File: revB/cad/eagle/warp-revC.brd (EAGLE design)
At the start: 38.1 x 38.1 mm, 148 parts, among them J3 QIIC connector, J4 DF40FC-20DP-0.4V(51)

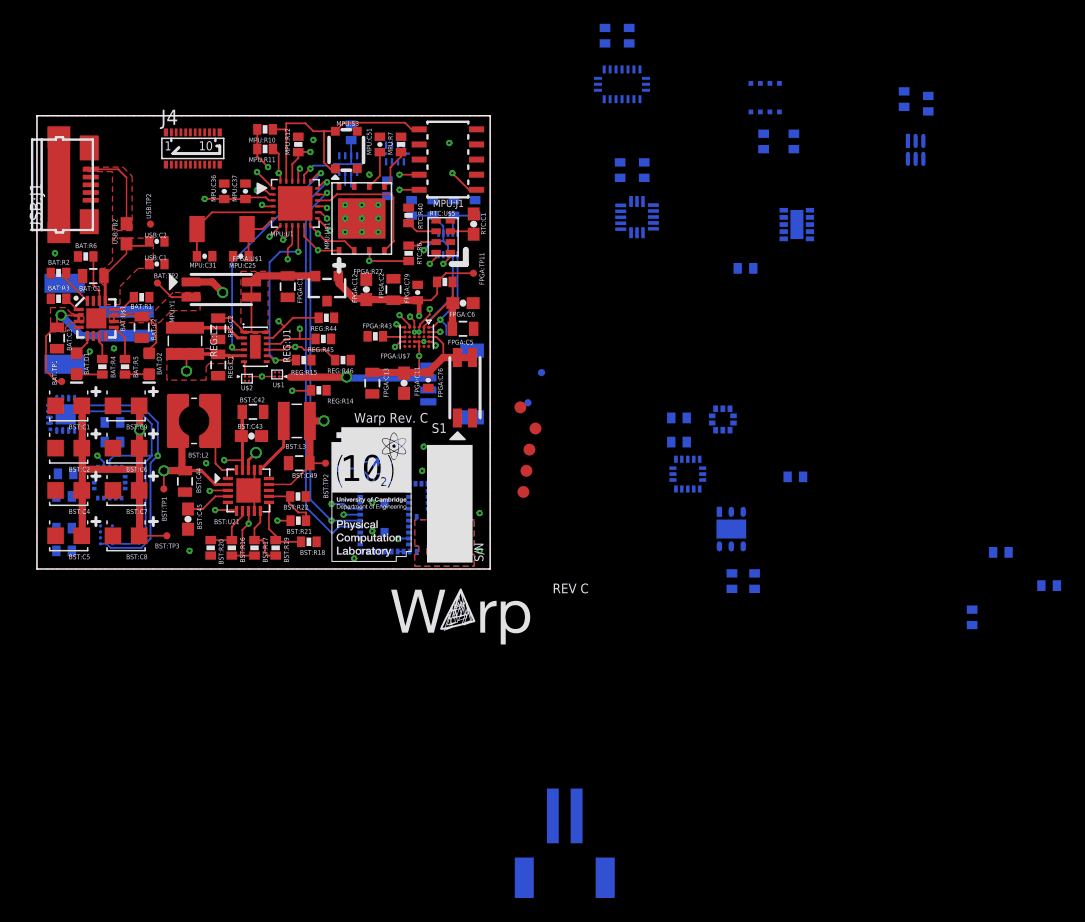
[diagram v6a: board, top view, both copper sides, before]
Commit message: Bottom sensor placement
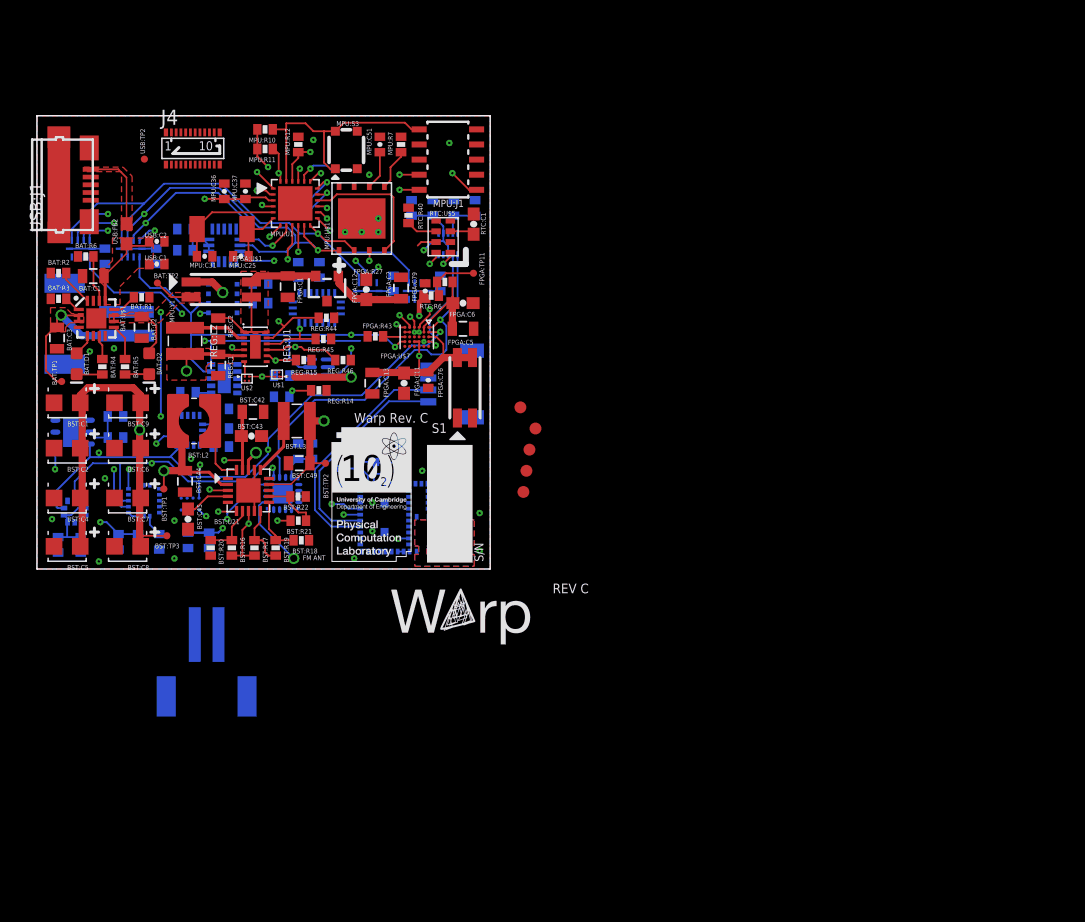
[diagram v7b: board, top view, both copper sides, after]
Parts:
- removed SEN1:C52, SEN1:C53: 0.1uF, SparkFun-Passives:0402-CAP
- removed SEN1:U20, SEN1:U23: ISL23415UTQFN, ISL23415:ISL23415
- removed SEN2:TP1, SEN2:TP2: TPTP06R, testpad:TP06R
- added DP:C1, DP:C2, DP:C52, DP:C53: 0.1uF, SparkFun-Passives:0402-CAP
- added DP:U1, DP:U2, DP:U20, DP:U23: ISL23415UTQFN, ISL23415:ISL23415
- moved SEN2:C46 70.8 mm to (15.5, 11.8)
- moved SEN2:C24 68.6 mm to (10.3, 2.29), turned to 270 degrees
- moved SEN2:C47 66.6 mm to (15.5, 13.5)
- moved SEN1:C28 59.7 mm to (20.6, 14.5), turned to 0 degrees
- moved SEN1:C29 57.3 mm to (20.6, 16.3), turned to 0 degrees
- moved SEN2:U9 56.0 mm to (3.05, 11.6), turned to 180 degrees
- moved SEN2:C22 55.1 mm to (6.60, 11.0), turned to 180 degrees
- moved SEN2:U16 55.0 mm to (3.17, 4.83)
- moved SEN2:C23 53.6 mm to (6.60, 12.8), turned to 180 degrees
- moved SEN1:U10 53.4 mm to (23.7, 17.0), turned to 180 degrees
- moved SEN2:C18 53.3 mm to (1.78, 2.03), turned to 270 degrees
- moved SEN2:C19 51.0 mm to (3.68, 2.03), turned to 270 degrees
- moved SEN1:U5 49.8 mm to (15.7, 16.0), turned to 0 degrees
- moved SEN1:U2 48.6 mm to (15.6, 22.7), turned to 0 degrees
- moved SEN2:C14 48.3 mm to (15.5, 10.3)
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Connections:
- removed net SEN2:SI4705_LPI: SEN2:TP1.TP, SEN2:U13.P$4
- removed net SI4705_!RST!: MPU:U1.P$14
- new net DP:ISL23415_SPI_CS: DP:U1.4, DP:U2.4, DP:U20.4, DP:U23.4
- net GND: now also DP:C1.2, DP:C2.2, DP:C52.2, DP:C53.2, DP:U1.9, DP:U2.9, DP:U20.9, DP:U23.9; no longer SEN1:C52.2, SEN1:C53.2, SEN1:U20.9, SEN1:U23.9
- net I2C1_SCL: now also DP:U20.6; no longer SEN1:U20.6
- net I2C1_SDA: now also DP:U23.6; no longer SEN1:U23.6
- net I2C2_SCL: now also DP:U1.6
- net I2C2_SDA: now also DP:U2.6
- net ISL23415_SPI_CS: no longer SEN1:U20.4, SEN1:U23.4
- net SEN2:SI4705_FMI: no longer SEN2:TP2.TP
- net SI4705_!RST: now also MPU:U1.P$14
- net SPI_MISO/UART_RTS: now also DP:U1.2, DP:U2.2, DP:U20.2, DP:U23.2; no longer SEN1:U20.2, SEN1:U23.2
- net SPI_MOSI/UART_CTS: now also DP:U1.3, DP:U2.3, DP:U20.3, DP:U23.3; no longer SEN1:U20.3, SEN1:U23.3
- net SPI_SCK: now also DP:U1.1, DP:U2.1, DP:U20.1, DP:U23.1; no longer SEN1:U20.1, SEN1:U23.1
- net VS2: now also DP:C1.1, DP:C2.1, DP:C52.1, DP:C53.1, DP:U1.10, DP:U1.5, DP:U1.8, DP:U2.10, DP:U2.5, DP:U2.8, DP:U20.10, DP:U20.5, DP:U20.8, DP:U23.10, DP:U23.5, DP:U23.8; no longer SEN1:C52.1, SEN1:C53.1, SEN1:U20.10, SEN1:U20.5, SEN1:U20.8, SEN1:U23.10, SEN1:U23.5, SEN1:U23.8
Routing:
- net VS2: track 22.3 -> 68.2 mm, vias 3 -> 6
- net SI4705_!RST: track 0.00 -> 42.8 mm, vias 0 -> 4
- net SPI_SCK: track 16.4 -> 58.5 mm
- net SPI_MISO/UART_RTS: track 36.5 -> 74.6 mm, vias 3 -> 6
- net I2C1_SDA: track 1.01 -> 38.4 mm, vias 1 -> 3
- net SPI_MOSI/UART_CTS: track 39.0 -> 75.9 mm, vias 3 -> 6
- net CLK32K: track 1.13 -> 35.6 mm
- net I2C1_SCL: track 0.73 -> 34.4 mm, vias 1 -> 4
- net I2C2_SCL: track 35.2 -> 68.7 mm, vias 3 -> 7
- net I2C2_SDA: track 32.2 -> 64.5 mm, vias 1 -> 4
- net REG_CTRL: track 28.2 -> 10.5 mm
- net REG_VSEL4: track 16.1 -> 4.83 mm
- net I2C0_SDA/UART_RX: track 36.0 -> 24.8 mm
- net I2C0_SCL/UART_TX: track 33.3 -> 22.6 mm, vias 3 -> 2
- net ADXL362_SPI_CS: track 0.87 -> 10.4 mm, vias 1 -> 2
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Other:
- board text added: "FM ANT"

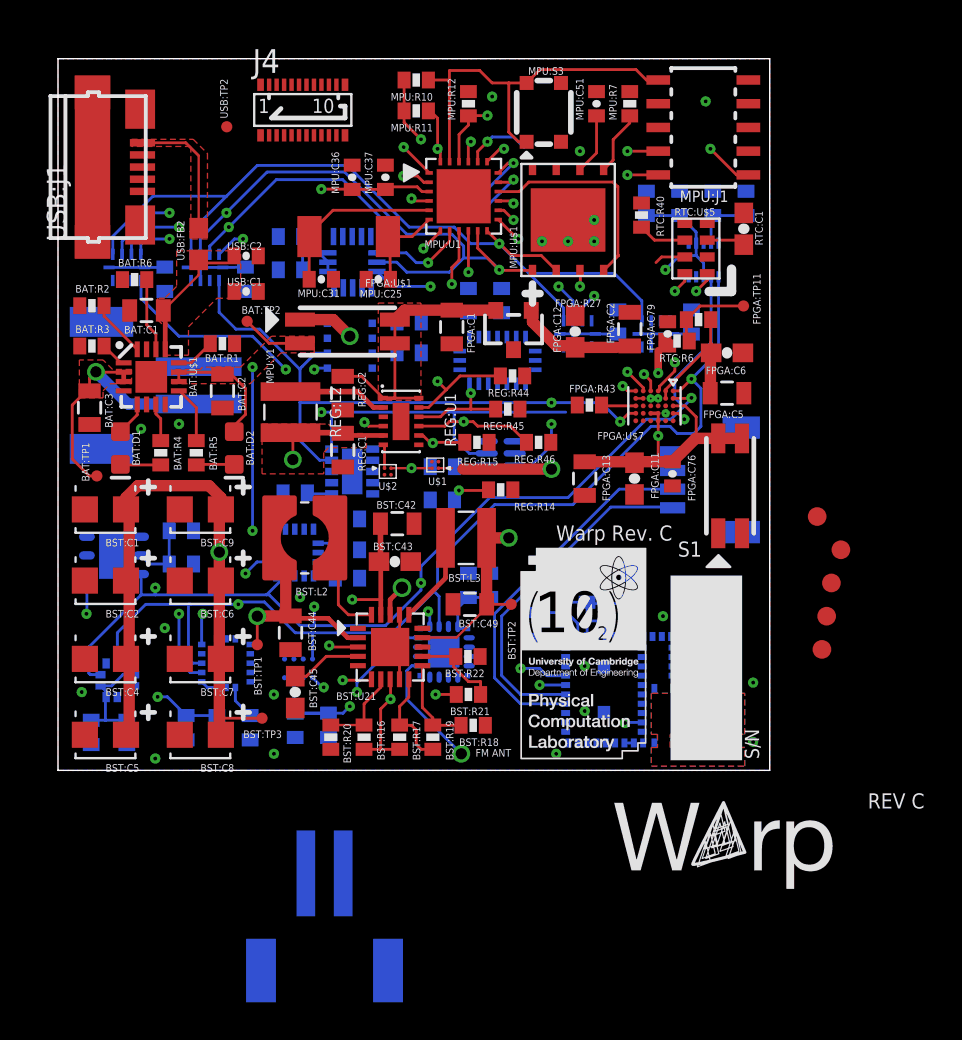
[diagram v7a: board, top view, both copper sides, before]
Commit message: All chips routed
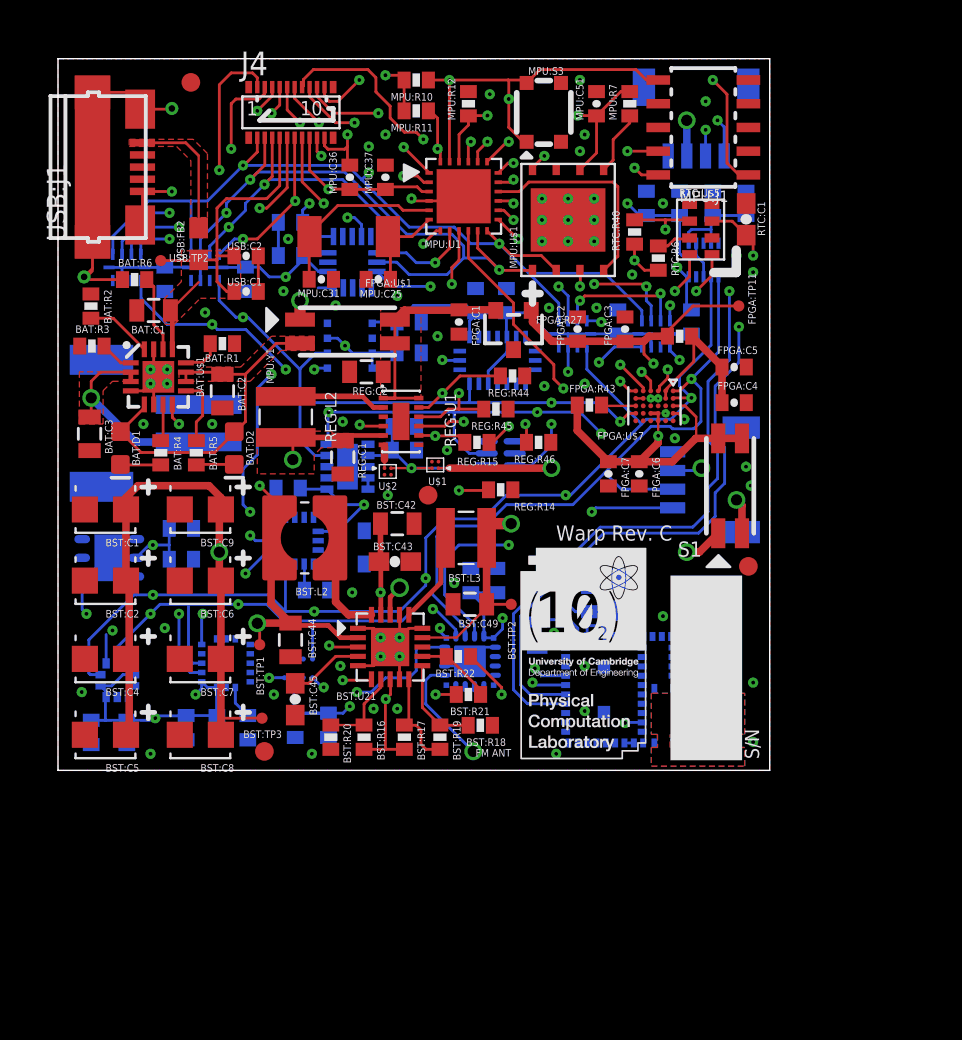
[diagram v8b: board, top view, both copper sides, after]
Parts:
- removed BAT:TP1, BAT:TP2: TPSTP06R, testpad:TP06R
- removed FD4: FIDUCIAL1X2, SparkFun-Aesthetics:FIDUCIAL-1X2
- removed FPGA:C11, FPGA:C12: 0.1uF, SparkFun-Passives:0603-CAP
- removed FPGA:C13: 1uF, SparkFun-Passives:0805
- removed FPGA:C76, FPGA:C79: 10nF, SparkFun-Passives:0402-CAP
- added FPGA:C3, FPGA:C4: 0.1uF, SparkFun-Passives:0402-CAP
- added FPGA:C7: 10uF, SparkFun-Passives:0402-CAP
- FPGA:C1, FPGA:C2, FPGA:C5: device SparkFun-Passives:0805 -> SparkFun-Passives:0402-CAP
- FPGA:C6: device SparkFun-Passives:0603-CAP -> SparkFun-Passives:0402-CAP
- J2: value (none) -> QIIC connector; device SparkFun-Connectors:JST-2-SMD -> SparkX:1X04_1MM_RA
- moved J2 46.6 mm to (34.2, 32.9)
- moved FD1 40.8 mm to (7.11, 36.8)
- moved FD5 31.7 mm to (11.0, 1.02)
- moved FD2 22.3 mm to (19.8, 14.7)
- moved FPGA:C6 8.00 mm to (31.1, 15.9), turned to 270 degrees
- moved USB:TP2 7.99 mm to (5.50, 27.3), turned to 270 degrees
- moved FD3 5.03 mm to (37.0, 10.9)
- moved RTC:R6 4.55 mm to (32.1, 27.4), turned to 270 degrees
- moved SEN1:C28 3.35 mm to (18.5, 17.1), turned to 180 degrees
- moved SEN1:C29 2.96 mm to (18.5, 18.4), turned to 180 degrees
- moved FPGA:C2 2.79 mm to (27.8, 23.6)
- moved SEN2:C47 2.43 mm to (15.7, 11.0)
- moved J1 2.03 mm to (3.83, 18.6)
- moved SEN2:C14 1.77 mm to (13.8, 9.65)
- moved REG:C2 1.71 mm to (16.5, 21.3), turned to 180 degrees
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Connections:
- removed net DP:ISL23415_SPI_CS: DP:U1.4, DP:U2.4, DP:U20.4, DP:U23.4
- net ADXL362_SPI_CS: no longer J4.P$18
- net BAT: no longer BAT:TP1.TP
- net BGX13S_!RST: now also J4.P$7; no longer J4.P$20
- net CHARGE_VOUT: no longer BAT:TP2.TP
- net FPGA:ICE40_VCC_PLL: now also FPGA:C4.1; no longer FPGA:C6.1
- net FPGA:VCC_1V2: now also FPGA:C3.1; no longer FPGA:C12.1, FPGA:C79.1
- net FPGA_VS: now also FPGA:C6.1, FPGA:C7.1; no longer FPGA:C11.1, FPGA:C13.1, FPGA:C76.1
- net GND: now also FPGA:C3.2, FPGA:C4.2, FPGA:C7.2, J4.P$20; no longer FPGA:C11.2, FPGA:C12.2, FPGA:C13.2, FPGA:C76.2, FPGA:C79.2, J4.P$1
- net I2C0_SCL/UART_TX: now also J4.P$5; no longer J3.4, J4.P$11
- net I2C0_SDA/UART_RX: now also J4.P$6; no longer J3.3, J4.P$12
- net I2C1_SCL: now also J2.4, J4.P$1; no longer J4.P$13
- net I2C1_SDA: now also J2.3, J4.P$2; no longer J4.P$14
- net I2C2_SCL: now also J3.4, J4.P$3; no longer J4.P$15
- net I2C2_SDA: now also J3.3, J4.P$4; no longer J4.P$16
- net ISL23415_SPI_CS: now also DP:U1.4, DP:U2.4, DP:U20.4, DP:U23.4, J4.P$16; no longer J4.P$17
- net PV_VS: now also J4.P$15; no longer J2.2, J4.P$4
- net RTC_!INT!/RESET_B: now also J4.P$10; no longer J4.P$7
- net SI4705_!RST: now also J4.P$17; no longer J4.P$19
- net SPI_MISO/UART_RTS: now also J4.P$12; no longer J4.P$9
- net SPI_MOSI/UART_CTS: now also J4.P$13; no longer J4.P$10
- net SPI_SCK: now also J4.P$11; no longer J4.P$8
- net SWD_CLK: now also J4.P$9; no longer J4.P$6
- net SWD_DIO: now also J4.P$8; no longer J4.P$5
- net USB_5V: now also J4.P$14; no longer J4.P$2
- net VCC_QIIC: now also J2.2
- net VS1: now also J4.P$18
- net VS2: now also J4.P$19; no longer J4.P$3
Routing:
- net I2C1_SCL: track 34.4 -> 95.9 mm, vias 4 -> 11
- net I2C2_SCL: track 68.7 -> 124.7 mm, vias 7 -> 10
- net VS2: track 68.2 -> 123.6 mm, vias 6 -> 17
- net GND: track 4.79 -> 57.8 mm, vias 20 -> 73
- net I2C2_SDA: track 64.5 -> 115.5 mm, vias 4 -> 7
- net ISL23415_SPI_CS: track 3.60 -> 48.4 mm, vias 1 -> 7
- net I2C1_SDA: track 38.4 -> 82.6 mm, vias 3 -> 7
- net I2C0_SCL/UART_TX: track 22.6 -> 64.8 mm, vias 2 -> 4
- net I2C0_SDA/UART_RX: track 24.8 -> 66.6 mm, vias 2 -> 4
- net REG_CTRL: track 10.5 -> 50.2 mm
- net VCC_QIIC: track 5.46 -> 37.0 mm, vias 1 -> 3
- net PV_VS: track 10.3 -> 35.3 mm, vias 1 -> 3
- net SPI_MOSI/UART_CTS: track 75.9 -> 98.4 mm, vias 6 -> 9
- net RTC_!INT!/RESET_B: track 24.7 -> 46.0 mm, vias 0 -> 4
- net REG_VSEL4: track 4.83 -> 22.3 mm
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- added copper zone on layer 14, net VS2
- removed copper zone on layer 14, net GND
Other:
- board text removed: "REV C"
